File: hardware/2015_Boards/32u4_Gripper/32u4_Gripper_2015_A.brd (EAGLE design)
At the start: 31.8 x 55.9 mm, 18 parts, among them U1 SN74LS241DW, U2 XBEE-1B3

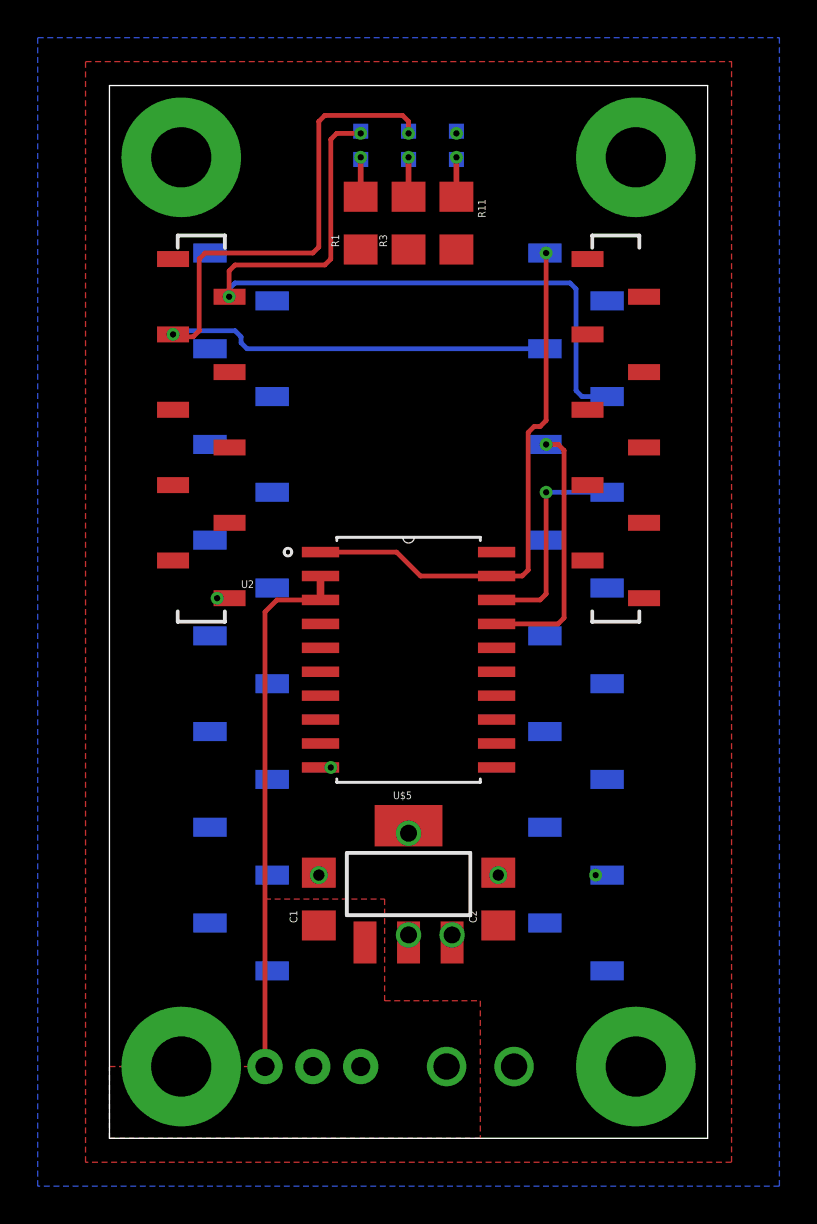
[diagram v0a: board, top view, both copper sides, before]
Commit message: Added breakout headers for forgotten sensors.
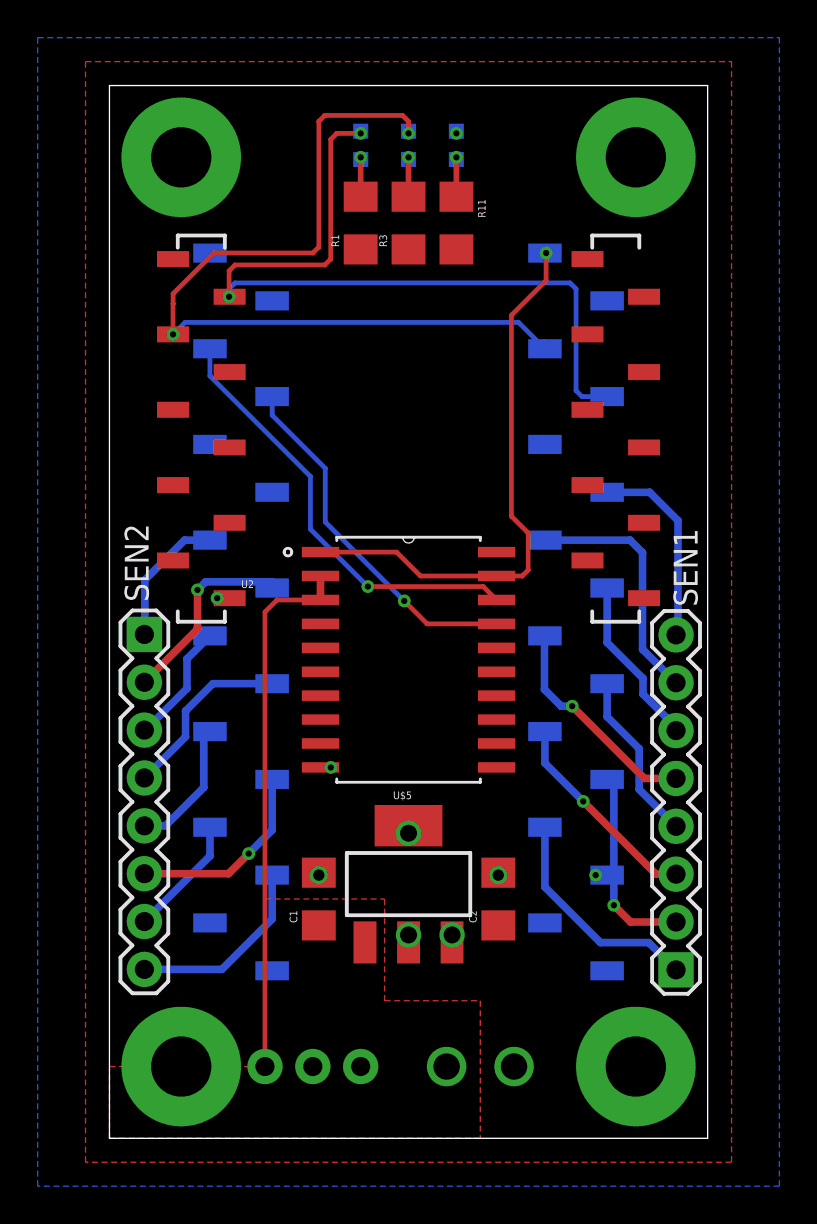
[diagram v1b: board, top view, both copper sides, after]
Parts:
- added SEN1, SEN2: (no value), SparkFun-Connectors:1X08
- C1, C2: value (none) -> 0.1uF
- renumbered JP1 to SERVO
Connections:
- new net N$10: SEN1.8, U$1.P$11
- new net N$11: SEN2.8, U$1.P$19
- new net N$12: SEN2.7, U$1.P$20
- new net N$13: SEN2.6, U$1.P$21
- new net N$14: SEN2.5, U$1.P$22
- new net N$15: SEN2.3, U$1.P$24
- new net N$16: SEN2.4, U$1.P$23
- new net N$17: SEN2.2, U$1.P$25
- new net N$18: SEN2.1, U$1.P$26
- new net N$2: SEN1.1, U$1.P$4
- new net N$3: SEN1.2, U$1.P$5
- new net N$5: SEN1.3, U$1.P$6
- new net N$6: SEN1.4, U$1.P$7
- new net N$7: SEN1.5, U$1.P$8
- new net N$8: SEN1.6, U$1.P$9
- new net N$9: SEN1.7, U$1.P$10
- net RX_1: now also U$1.P$30; no longer U$1.P$11
- net TX_1: now also U$1.P$29; no longer U$1.P$12
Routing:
- net N$9: track 0.00 -> 13.1 mm
- net N$2: track 0.00 -> 12.0 mm
- net RX_1: track 11.4 -> 23.2 mm
- net N$7: track 0.00 -> 11.8 mm, vias 0 -> 1
- net N$5: track 0.00 -> 11.1 mm, vias 0 -> 1
- net N$17: track 0.00 -> 10.5 mm, vias 0 -> 1
- net N$3: track 0.00 -> 10.5 mm, vias 0 -> 1
- net N$10: track 0.00 -> 10.5 mm
- net N$13: track 0.00 -> 10.4 mm, vias 0 -> 1
- net N$11: track 0.00 -> 10.2 mm
- net N$16: track 0.00 -> 9.66 mm
- net N$8: track 0.00 -> 9.08 mm
- net N$6: track 0.00 -> 9.08 mm
- net N$18: track 0.00 -> 7.23 mm
- net N$14: track 0.00 -> 7.10 mm
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
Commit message: Fixed Traces
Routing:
- net N$10: track 10.5 -> 9.08 mm
- net N$18: track 7.23 -> 6.45 mm
- net N$9: track 13.1 -> 12.5 mm
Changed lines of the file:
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@@
 <contactref element="SEN1" pad="5"/>
 <wire x1="23.114" y1="26.67" x2="23.0886" y2="26.6446" width="0.4064" layer="16"/>
-<wire x1="23.0886" y1="26.6446" x2="23.0886" y2="23.8252" width="0.4064" layer="16"/>
-<wire x1="23.0886" y1="23.8252" x2="23.9776" y2="22.9362" width="0.4064" layer="16"/>
-<wire x1="23.9776" y1="22.9362" x2="24.5618" y2="22.9362" width="0.4064" layer="16"/>
 <via x="24.5618" y="22.9362" extent="1-16" drill="0.3302"/>
 <wire x1="24.5618" y1="22.9362" x2="28.3972" y2="19.1008" width="0.4064" layer="1"/>
 <wire x1="28.3972" y1="19.1008" x2="30.0736" y2="19.1008" width="0.4064" layer="1"/>
+<wire x1="24.5618" y1="22.9362" x2="23.114" y2="24.384" width="0.4064" layer="16"/>
+<wire x1="23.114" y1="24.384" x2="23.114" y2="26.67" width="0.4064" layer="16"/>
 </signal>
 <signal name="N$8">
@@
 <contactref element="U$1" pad="P$10"/>
 <contactref element="SEN1" pad="7"/>
-<wire x1="23.114" y1="31.75" x2="27.6352" y2="31.75" width="0.4064" layer="16"/>
-<wire x1="27.6352" y1="31.75" x2="28.2956" y2="31.0896" width="0.4064" layer="16"/>
-<wire x1="28.2956" y1="31.0896" x2="28.2956" y2="25.9588" width="0.4064" layer="16"/>
-<wire x1="28.2956" y1="25.9588" x2="30.0736" y2="24.1808" width="0.4064" layer="16"/>
+<wire x1="28.067" y1="26.1874" x2="30.0736" y2="24.1808" width="0.4064" layer="16"/>
+<wire x1="23.114" y1="31.75" x2="26.5684" y2="31.75" width="0.4064" layer="16"/>
+<wire x1="26.5684" y1="31.75" x2="28.067" y2="30.2514" width="0.4064" layer="16"/>
+<wire x1="28.067" y1="30.2514" x2="28.067" y2="26.1874" width="0.4064" layer="16"/>
 </signal>
 <signal name="N$10">
 <contactref element="SEN1" pad="8"/>
 <contactref element="U$1" pad="P$11"/>
-<wire x1="26.416" y1="34.29" x2="28.6766" y2="34.29" width="0.4064" layer="16"/>
-<wire x1="28.6766" y1="34.29" x2="30.1752" y2="32.7914" width="0.4064" layer="16"/>
-<wire x1="30.1752" y1="32.7914" x2="30.1752" y2="26.8224" width="0.4064" layer="16"/>
-<wire x1="30.1752" y1="26.8224" x2="30.0736" y2="26.7208" width="0.4064" layer="16"/>
+<wire x1="26.416" y1="34.29" x2="30.0736" y2="30.6324" width="0.4064" layer="16"/>
+<wire x1="30.0736" y1="30.6324" x2="30.0736" y2="26.7208" width="0.4064" layer="16"/>
 </signal>
 <signal name="N$11">
@@
 <contactref element="SEN2" pad="1"/>
 <contactref element="U$1" pad="P$26"/>
-<wire x1="1.8542" y1="26.7462" x2="1.8796" y2="26.7716" width="0.4064" layer="16"/>
-<wire x1="1.8796" y1="26.7716" x2="1.8796" y2="29.6418" width="0.4064" layer="16"/>
-<wire x1="1.8796" y1="29.6418" x2="3.9878" y2="31.75" width="0.4064" layer="16"/>
-<wire x1="3.9878" y1="31.75" x2="5.334" y2="31.75" width="0.4064" layer="16"/>
+<wire x1="5.334" y1="31.75" x2="1.8542" y2="28.2702" width="0.4064" layer="16"/>
+<wire x1="1.8542" y1="28.2702" x2="1.8542" y2="26.7462" width="0.4064" layer="16"/>
 </signal>
 </signals>

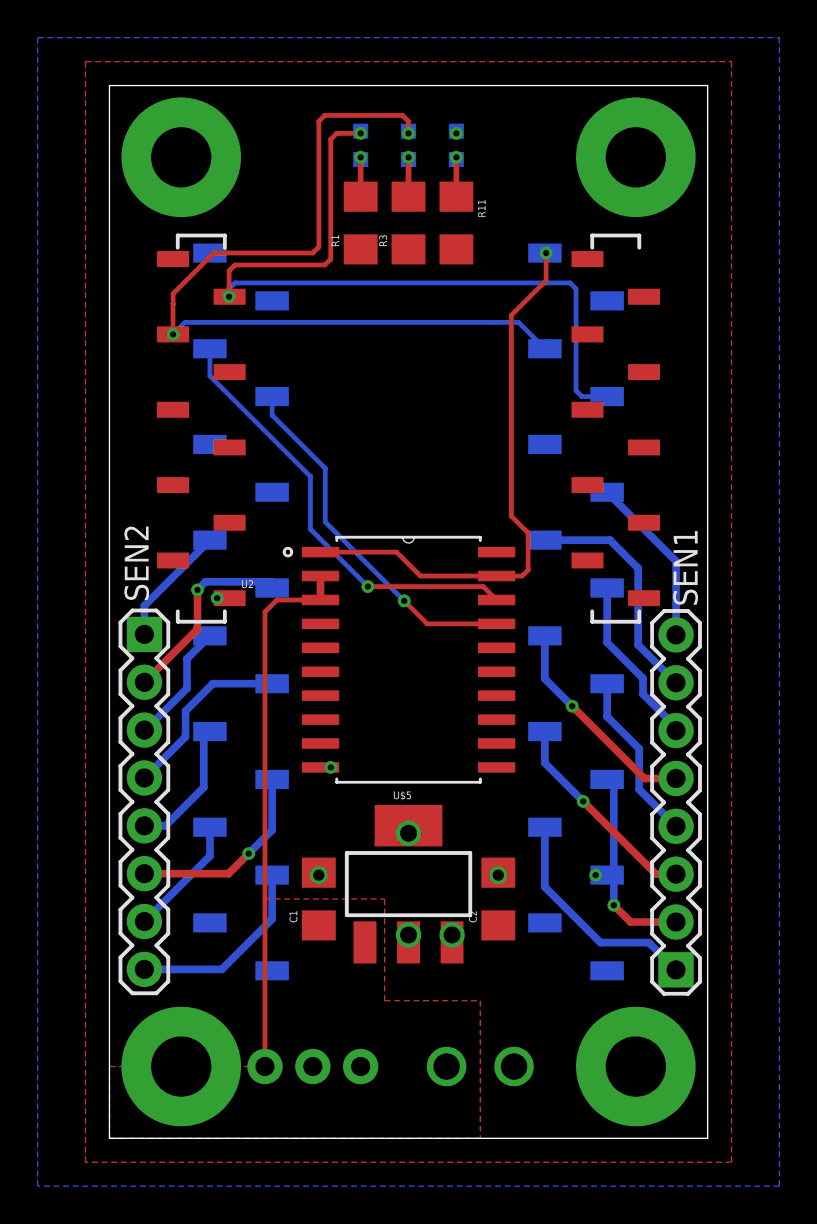
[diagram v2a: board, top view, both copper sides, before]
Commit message: Added 3.3V and GND breakout
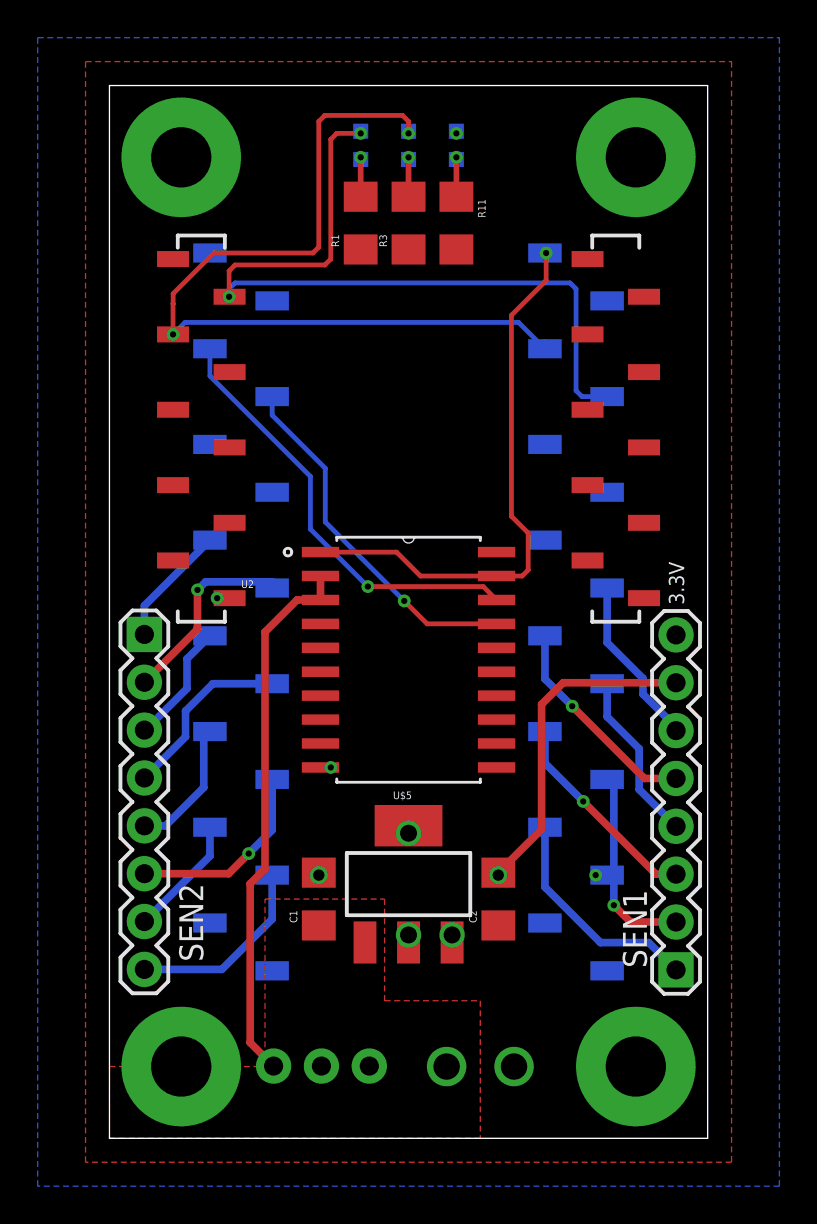
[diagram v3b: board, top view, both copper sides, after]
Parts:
- U$3: value H_WR-TBL_321*0002VERT -> PLUGABLE SCREW TERMINALS
- moved SERVO 0.46 mm to (8.71, 3.84)
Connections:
- removed net N$10: SEN1.8, U$1.P$11
- removed net N$9: SEN1.7, U$1.P$10
- net 3.3V: now also SEN1.8
- net GND: now also SEN1.7
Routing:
- net GND: track 3.73 -> 21.2 mm
- net N$9: track 12.5 -> 0.00 mm
- net N$10: track 9.08 -> 0.00 mm
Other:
- board text added: "3.3V"
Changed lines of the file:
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@@
 <dimension x1="0" y1="55.88" x2="0" y2="0" x3="-5.08" y3="27.94" textsize="1.778" layer="25" unit="inch" precision="5"/>
 <dimension x1="0" y1="55.88" x2="31.75" y2="55.88" x3="15.875" y3="59.69" textsize="1.778" layer="25" unit="inch" precision="5"/>
+<text x="30.5054" y="28.321" size="0.8128" layer="21" rot="R90">3.3V</text>
 </plain>
 <attributes>
@@
 </autorouter>
 <elements>
-<element name="SERVO" library="SparkFun-Connectors" package="1X03" value="" x="8.255" y="3.81" smashed="yes" rot="MR180">
-<attribute name="VALUE" x="6.985" y="6.985" size="1.27" layer="28" rot="MR180"/>
+<element name="SERVO" library="SparkFun-Connectors" package="1X03" value="" x="8.7122" y="3.8354" smashed="yes" rot="MR180">
+<attribute name="VALUE" x="7.4422" y="7.0104" size="1.27" layer="28" rot="MR180"/>
 </element>
 <element name="LED1" library="SparkFun" package="LED-0603" value="Red" x="18.415" y="52.705" rot="MR0"/>
@@
 <element name="R3" library="SparkFun-Passives" package="1206" value="1k" x="15.875" y="48.5775" rot="R90"/>
 <element name="U$1" library="MRDT-2015-General" package="32U3_MCU_DIP_SMD" value="32U4_BREAKOU_SMD" x="15.875" y="27.94" rot="MR0"/>
-<element name="U$3" library="MRDT-2015-PowerBoard" package="691321100002" value="H_WR-TBL_321*0002VERT" x="19.685" y="3.81" rot="MR180">
+<element name="U$3" library="MRDT-2015-PowerBoard" package="691321100002" value="PLUGABLE SCREW TERMINALS" x="19.685" y="3.81" rot="MR180">
 <attribute name="DIGIKEY_PN" value="732-2763-ND" x="19.685" y="3.81" size="1.778" layer="28" rot="MR180" display="off"/>
 </element>
@@
 <element name="C2" library="SparkFun-Passives" package="1206" value="0.1uF" x="20.6375" y="12.7" rot="R90"/>
 <element name="SEN1" library="SparkFun-Connectors" package="1X08" value="" x="30.0736" y="8.9408" smashed="yes" rot="R90">
-<attribute name="NAME" x="31.2166" y="28.2194" size="1.27" layer="25" ratio="10" rot="R90"/>
+<attribute name="NAME" x="28.5242" y="9.0424" size="1.27" layer="25" ratio="10" rot="R90"/>
 <attribute name="VALUE" x="33.2486" y="7.6708" size="1.27" layer="27" rot="R90"/>
 </element>
 <element name="SEN2" library="SparkFun-Connectors" package="1X08" value="" x="1.8542" y="26.7462" smashed="yes" rot="R270">
-<attribute name="NAME" x="2.0828" y="28.4734" size="1.27" layer="25" ratio="10" rot="R90"/>
+<attribute name="NAME" x="4.9784" y="9.3726" size="1.27" layer="25" ratio="10" rot="R90"/>
 <attribute name="VALUE" x="-1.3208" y="28.0162" size="1.27" layer="27" rot="R270"/>
 </element>
@@
 <wire x1="11.1125" y1="14.1" x2="11.1125" y2="13.97" width="0.4064" layer="1"/>
 <wire x1="20.6375" y1="14.1" x2="20.6375" y2="13.97" width="0.4064" layer="1"/>
+<contactref element="SEN1" pad="7"/>
+<wire x1="20.6375" y1="14.1" x2="22.9362" y2="16.3987" width="0.4064" layer="1"/>
+<wire x1="22.9362" y1="16.3987" x2="22.9362" y2="23.0378" width="0.4064" layer="1"/>
+<wire x1="24.0792" y1="24.1808" x2="30.0736" y2="24.1808" width="0.4064" layer="1"/>
+<wire x1="22.9362" y1="23.0378" x2="24.0792" y2="24.1808" width="0.4064" layer="1"/>
 </signal>
 <signal name="RESET">
@@
 <wire x1="25.8064" y1="13.97" x2="26.416" y2="13.97" width="0.3048" layer="16"/>
 <contactref element="C2" pad="1"/>
+<contactref element="SEN1" pad="8"/>
 </signal>
 <signal name="DIO4">
@@
 <contactref element="U1" pad="3"/>
 <contactref element="SERVO" pad="1"/>
+<wire x1="11.2014" y1="28.575" x2="9.9568" y2="28.575" width="0.4064" layer="1"/>
+<wire x1="9.9568" y1="28.575" x2="8.255" y2="26.8732" width="0.4064" layer="1"/>
 <wire x1="11.2014" y1="29.845" x2="11.2014" y2="28.575" width="0.4064" layer="1"/>
-<wire x1="8.255" y1="27.94" x2="8.89" y2="28.575" width="0.254" layer="1"/>
-<wire x1="8.89" y1="28.575" x2="11.2014" y2="28.575" width="0.254" layer="1"/>
-<wire x1="8.255" y1="27.94" x2="8.255" y2="3.81" width="0.254" layer="1"/>
+<wire x1="8.7122" y1="3.8354" x2="7.4676" y2="5.08" width="0.4064" layer="1"/>
+<wire x1="7.4676" y1="5.08" x2="7.4676" y2="13.5128" width="0.4064" layer="1"/>
+<wire x1="8.255" y1="26.8732" x2="8.255" y2="14.3002" width="0.4064" layer="1"/>
+<wire x1="8.255" y1="14.3002" x2="7.4676" y2="13.5128" width="0.4064" layer="1"/>
 </signal>
 <signal name="RX_1">
@@
 <wire x1="30.0736" y1="21.8186" x2="30.0736" y2="21.6408" width="0.4064" layer="16"/>
 </signal>
-<signal name="N$9">
-<contactref element="U$1" pad="P$10"/>
-<contactref element="SEN1" pad="7"/>
-<wire x1="28.067" y1="26.1874" x2="30.0736" y2="24.1808" width="0.4064" layer="16"/>
-<wire x1="23.114" y1="31.75" x2="26.5684" y2="31.75" width="0.4064" layer="16"/>
-<wire x1="26.5684" y1="31.75" x2="28.067" y2="30.2514" width="0.4064" layer="16"/>
-<wire x1="28.067" y1="30.2514" x2="28.067" y2="26.1874" width="0.4064" layer="16"/>
-</signal>
-<signal name="N$10">
-<contactref element="SEN1" pad="8"/>
-<contactref element="U$1" pad="P$11"/>
-<wire x1="26.416" y1="34.29" x2="30.0736" y2="30.6324" width="0.4064" layer="16"/>
-<wire x1="30.0736" y1="30.6324" x2="30.0736" y2="26.7208" width="0.4064" layer="16"/>
-</signal>
 <signal name="N$11">
